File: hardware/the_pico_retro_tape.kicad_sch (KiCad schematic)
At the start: 6 parts, among them U1 Pico

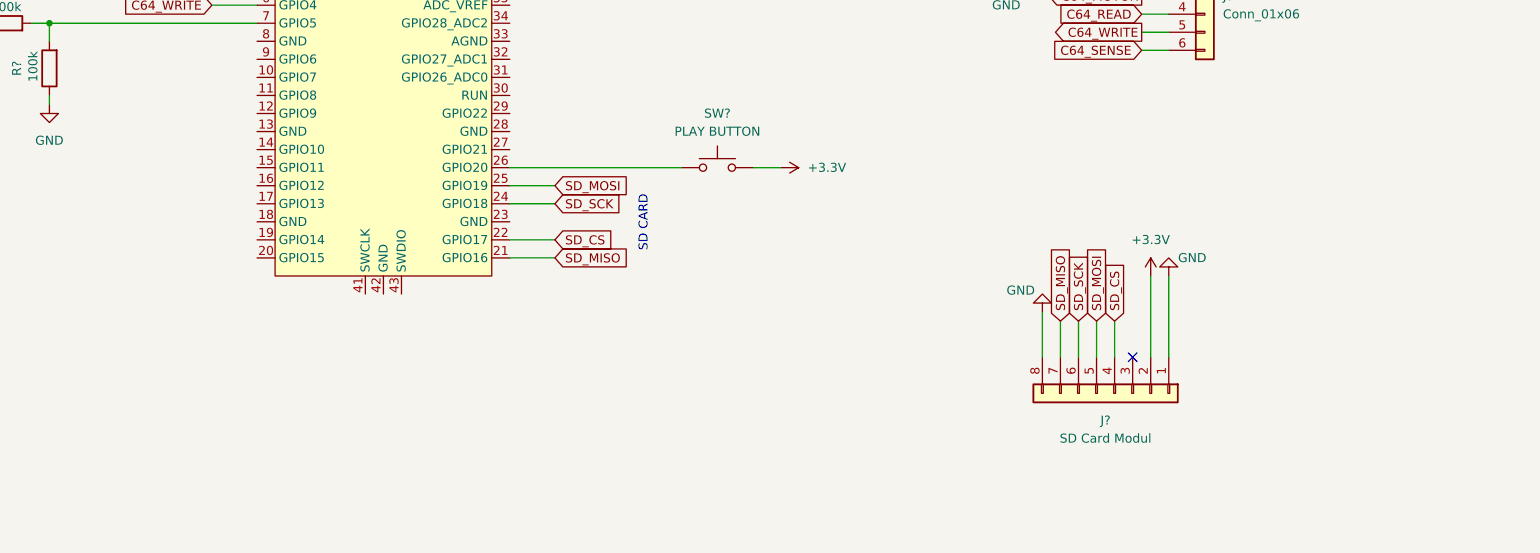
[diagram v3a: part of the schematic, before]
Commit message: hardware: added the tft display st7735 on spi1
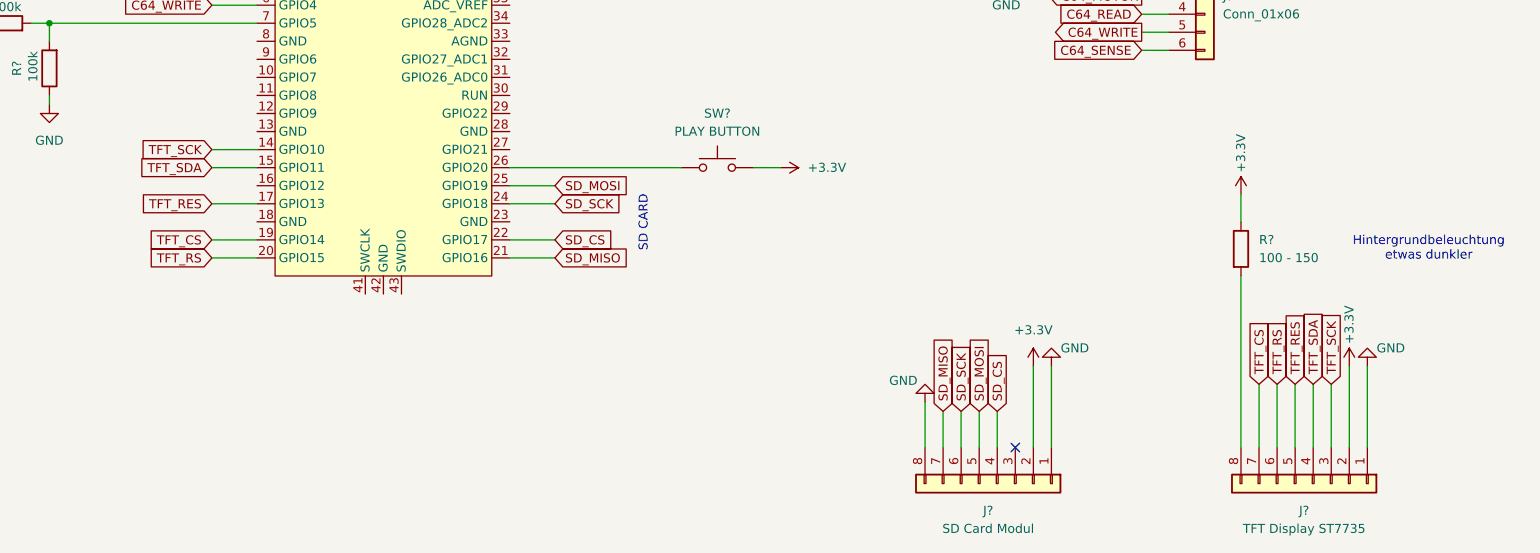
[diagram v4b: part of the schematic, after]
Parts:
- added J?: TFT Display ST7735, symbol Connector_Generic:Conn_01x08
- added R?: 100 - 150, symbol Device:R
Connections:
- net +3.3V: now also J?.2 (Pin_2), R?.1
- net GND: now also J?.1 (Pin_1)
- net TFT_SCK: now reaches U1.14 (GPIO10)
- net TFT_SCK: now also J?.3 (Pin_3)
- net TFT_SDA: now reaches U1.15 (GPIO11)
- net TFT_SDA: now also J?.4 (Pin_4)
- net TFT_RES: now reaches U1.17 (GPIO13)
- net TFT_RES: now also J?.5 (Pin_5)
- net TFT_CS: now reaches U1.19 (GPIO14)
- net TFT_CS: now also J?.7 (Pin_7)
- net TFT_RS: now reaches U1.20 (GPIO15)
- net TFT_RS: now also J?.6 (Pin_6)
- new net: J?.8 (Pin_8), R?.2
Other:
- note added: "Hintergrundbeleuchtung etwas dunkler"
- moved on the sheet: J?

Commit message: hardware: change tft vcc and led from 3.3v to 5v
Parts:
- R?: value 100 - 150 -> 150
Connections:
- net +3.3V: no longer J?.2 (Pin_2), R?.1
- net +5V: now also J?.2 (Pin_2), J?.2 (Pin_2), R?.1
- no-connect marks 2 -> 1
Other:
- note removed: "Hintergrundbeleuchtung etwas dunkler"
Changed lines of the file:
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@@
 		(at 195.58 123.19)
 	)
-	(no_connect
-		(at 217.17 57.15)
-	)
 	(wire
 		(pts
@@
 		(pts
 			(xy 245.11 111.76) (xy 245.11 123.19)
+		)
+		(stroke
+			(width 0)
+			(type default)
+		)
+	)
+	(wire
+		(pts
+			(xy 213.36 57.15) (xy 217.17 57.15)
 		)
 		(stroke
@@
 		(exclude_from_sim no)
 		(at 143.256 91.694 90)
-		(effects
-			(font
-				(size 1.27 1.27)
-			)
-		)
-	)
-	(text "Hintergrundbeleuchtung\netwas dunkler"
-		(exclude_from_sim no)
-		(at 253.746 95.25 0)
 		(effects
 			(font
@@
 	)
 	(symbol
+		(lib_id "power:+5V")
+		(at 213.36 57.15 90)
+		(unit 1)
+		(exclude_from_sim no)
+		(in_bom yes)
+		(on_board yes)
+		(dnp no)
+		(fields_autoplaced yes)
+		(property "Reference" "#PWR013"
+			(at 217.17 57.15 0)
+			(effects
+				(font
+					(size 1.27 1.27)
+				)
+				(hide yes)
+			)
+		)
+		(property "Value" "+5V"
+			(at 209.55 57.1499 90)
+			(effects
+				(font
+					(size 1.27 1.27)
+				)
+				(justify left)
+			)
+		)
+		(property "Footprint" ""
+			(at 213.36 57.15 0)
+			(effects
+				(font
+					(size 1.27 1.27)
+				)
+				(hide yes)
+			)
+		)
+		(property "Datasheet" ""
+			(at 213.36 57.15 0)
+			(effects
+				(font
+					(size 1.27 1.27)
+				)
+				(hide yes)
+			)
+		)
+		(property "Description" "Power symbol creates a global label with name \"+5V\""
+			(at 213.36 57.15 0)
+			(effects
+				(font
+					(size 1.27 1.27)
+				)
+				(hide yes)
+			)
+		)
+		(pin "1"
+		)
+		(instances
+			(project "the_pico_retro_tape"
+				(path "/58eb91ea-7f3f-48ec-bf75-2e4d8bc1bbc2"
+					(reference "#PWR013")
+					(unit 1)
+				)
+			)
+		)
+	)
+	(symbol
 		(lib_id "power:+3.3V")
 		(at 133.35 58.42 270)
@@
 	)
 	(symbol
-		(lib_id "power:+3.3V")
-		(at 227.33 87.63 0)
-		(unit 1)
-		(exclude_from_sim no)
-		(in_bom yes)
-		(on_board yes)
-		(dnp no)
-		(property "Reference" "#PWR012"
-			(at 227.33 91.44 0)
-			(effects
-				(font
-					(size 1.27 1.27)
-				)
-				(hide yes)
-			)
-		)
-		(property "Value" "+3.3V"
-			(at 227.33 81.788 90)
-			(effects
-				(font
-					(size 1.27 1.27)
-				)
-			)
-		)
-		(property "Footprint" ""
-			(at 227.33 87.63 0)
-			(effects
-				(font
-					(size 1.27 1.27)
-				)
-				(hide yes)
-			)
-		)
-		(property "Datasheet" ""
-			(at 227.33 87.63 0)
-			(effects
-				(font
-					(size 1.27 1.27)
-				)
-				(hide yes)
-			)
-		)
-		(property "Description" "Power symbol creates a global label with name \"+3.3V\""
-			(at 227.33 87.63 0)
-			(effects
-				(font
-					(size 1.27 1.27)
-				)
-				(hide yes)
-			)
-		)
-		(pin "1"
-		)
-		(instances
-			(project "the_pico_retro_tape"
-				(path "/58eb91ea-7f3f-48ec-bf75-2e4d8bc1bbc2"
-					(reference "#PWR012")
-					(unit 1)
-				)
-			)
-		)
-	)
-	(symbol
 		(lib_id "Switch:SW_Push")
 		(at 153.67 83.82 0)
@@
 				(path "/58eb91ea-7f3f-48ec-bf75-2e4d8bc1bbc2"
 					(reference "SW?")
+					(unit 1)
+				)
+			)
+		)
+	)
+	(symbol
+		(lib_id "power:+5V")
+		(at 242.57 111.76 0)
+		(unit 1)
+		(exclude_from_sim no)
+		(in_bom yes)
+		(on_board yes)
+		(dnp no)
+		(property "Reference" "#PWR012"
+			(at 242.57 115.57 0)
+			(effects
+				(font
+					(size 1.27 1.27)
+				)
+				(hide yes)
+			)
+		)
+		(property "Value" "+5V"
+			(at 242.57 106.68 90)
+			(effects
+				(font
+					(size 1.27 1.27)
+				)
+			)
+		)
+		(property "Footprint" ""
+			(at 242.57 111.76 0)
+			(effects
+				(font
+					(size 1.27 1.27)
+				)
+				(hide yes)
+			)
+		)
+		(property "Datasheet" ""
+			(at 242.57 111.76 0)
+			(effects
+				(font
+					(size 1.27 1.27)
+				)
+				(hide yes)
+			)
+		)
+		(property "Description" "Power symbol creates a global label with name \"+5V\""
+			(at 242.57 111.76 0)
+			(effects
+				(font
+					(size 1.27 1.27)
+				)
+				(hide yes)
+			)
+		)
+		(pin "1"
+		)
+		(instances
+			(project "the_pico_retro_tape"
+				(path "/58eb91ea-7f3f-48ec-bf75-2e4d8bc1bbc2"
+					(reference "#PWR012")
 					(unit 1)
 				)
@@
 	)
 	(symbol
-		(lib_id "power:+3.3V")
-		(at 242.57 111.76 0)
-		(unit 1)
-		(exclude_from_sim no)
-		(in_bom yes)
-		(on_board yes)
-		(dnp no)
-		(property "Reference" "#PWR011"
-			(at 242.57 115.57 0)
-			(effects
-				(font
-					(size 1.27 1.27)
-				)
-				(hide yes)
-			)
-		)
-		(property "Value" "+3.3V"
-			(at 242.57 105.918 90)
-			(effects
-				(font
-					(size 1.27 1.27)
-				)
-			)
-		)
-		(property "Footprint" ""
-			(at 242.57 111.76 0)
-			(effects
-				(font
-					(size 1.27 1.27)
-				)
-				(hide yes)
-			)
-		)
-		(property "Datasheet" ""
-			(at 242.57 111.76 0)
-			(effects
-				(font
-					(size 1.27 1.27)
-				)
-				(hide yes)
-			)
-		)
-		(property "Description" "Power symbol creates a global label with name \"+3.3V\""
-			(at 242.57 111.76 0)
-			(effects
-				(font
-					(size 1.27 1.27)
-				)
-				(hide yes)
-			)
-		)
-		(pin "1"
-		)
-		(instances
-			(project "the_pico_retro_tape"
-				(path "/58eb91ea-7f3f-48ec-bf75-2e4d8bc1bbc2"
-					(reference "#PWR011")
-					(unit 1)
-				)
-			)
-		)
-	)
-	(symbol
 		(lib_id "Device:R")
 		(at 227.33 95.25 0)
@@
 			)
 		)
-		(property "Value" "100 - 150"
+		(property "Value" "150"
 			(at 229.87 96.5199 0)
 			(effects
@@
 					(unit 1)
 				)
+			)
+		)
+	)
+	(symbol
+		(lib_id "power:+5V")
+		(at 227.33 87.63 0)
+		(unit 1)
+		(exclude_from_sim no)
+		(in_bom yes)
+		(on_board yes)
+		(dnp no)
+		(fields_autoplaced yes)
+		(property "Reference" "#PWR011"
+			(at 227.33 91.44 0)
+			(effects
+				(font
+					(size 1.27 1.27)
+				)
+				(hide yes)
+			)
+		)
+		(property "Value" "+5V"
+			(at 227.33 82.55 0)
+			(effects
+				(font
+					(size 1.27 1.27)
+				)
+			)
+		)
+		(property "Footprint" ""
+			(at 227.33 87.63 0)
+			(effects
+				(font
+					(size 1.27 1.27)
+				)
+				(hide yes)
+			)
+		)
+		(property "Datasheet" ""
+			(at 227.33 87.63 0)
+			(effects
+				(font
+					(size 1.27 1.27)
+				)
+				(hide yes)
+			)
+		)
+		(property "Description" "Power symbol creates a global label with name \"+5V\""
+			(at 227.33 87.63 0)
+			(effects
+				(font
+					(size 1.27 1.27)
+				)
+				(hide yes)
+			)
+		)
+		(pin "1"
+		)
+		(instances
+			(project "the_pico_retro_tape"
+				(path "/58eb91ea-7f3f-48ec-bf75-2e4d8bc1bbc2"
+					(reference "#PWR011")
+					(unit 1)
+				)

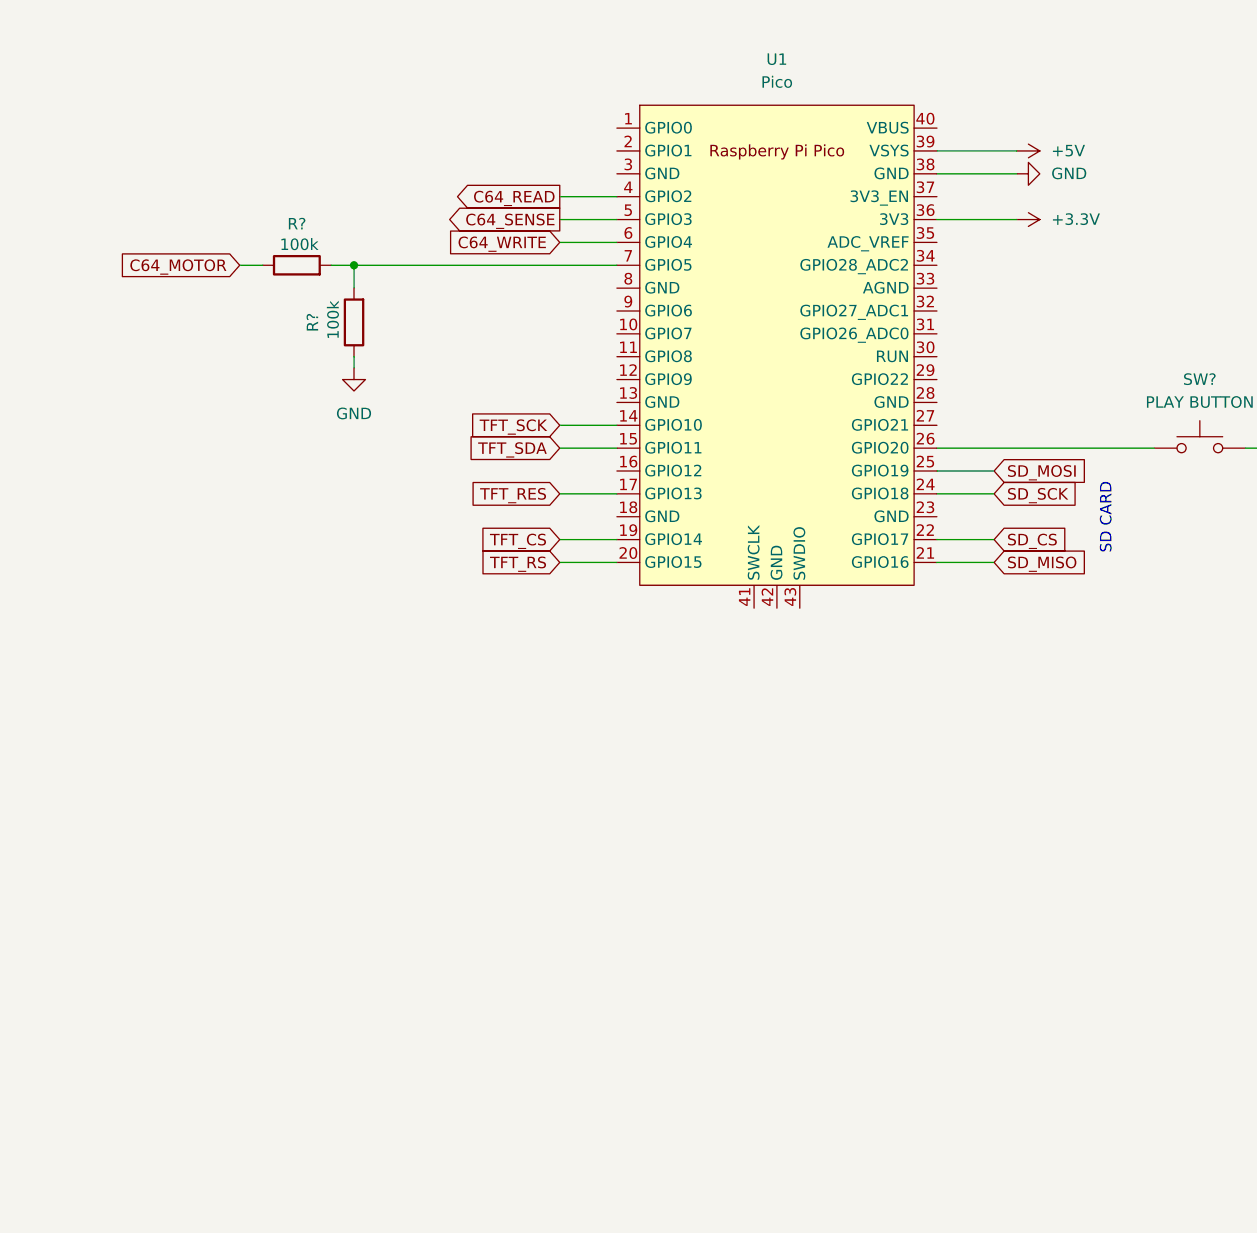
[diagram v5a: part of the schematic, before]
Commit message: hardware: added 3 buttons for gui
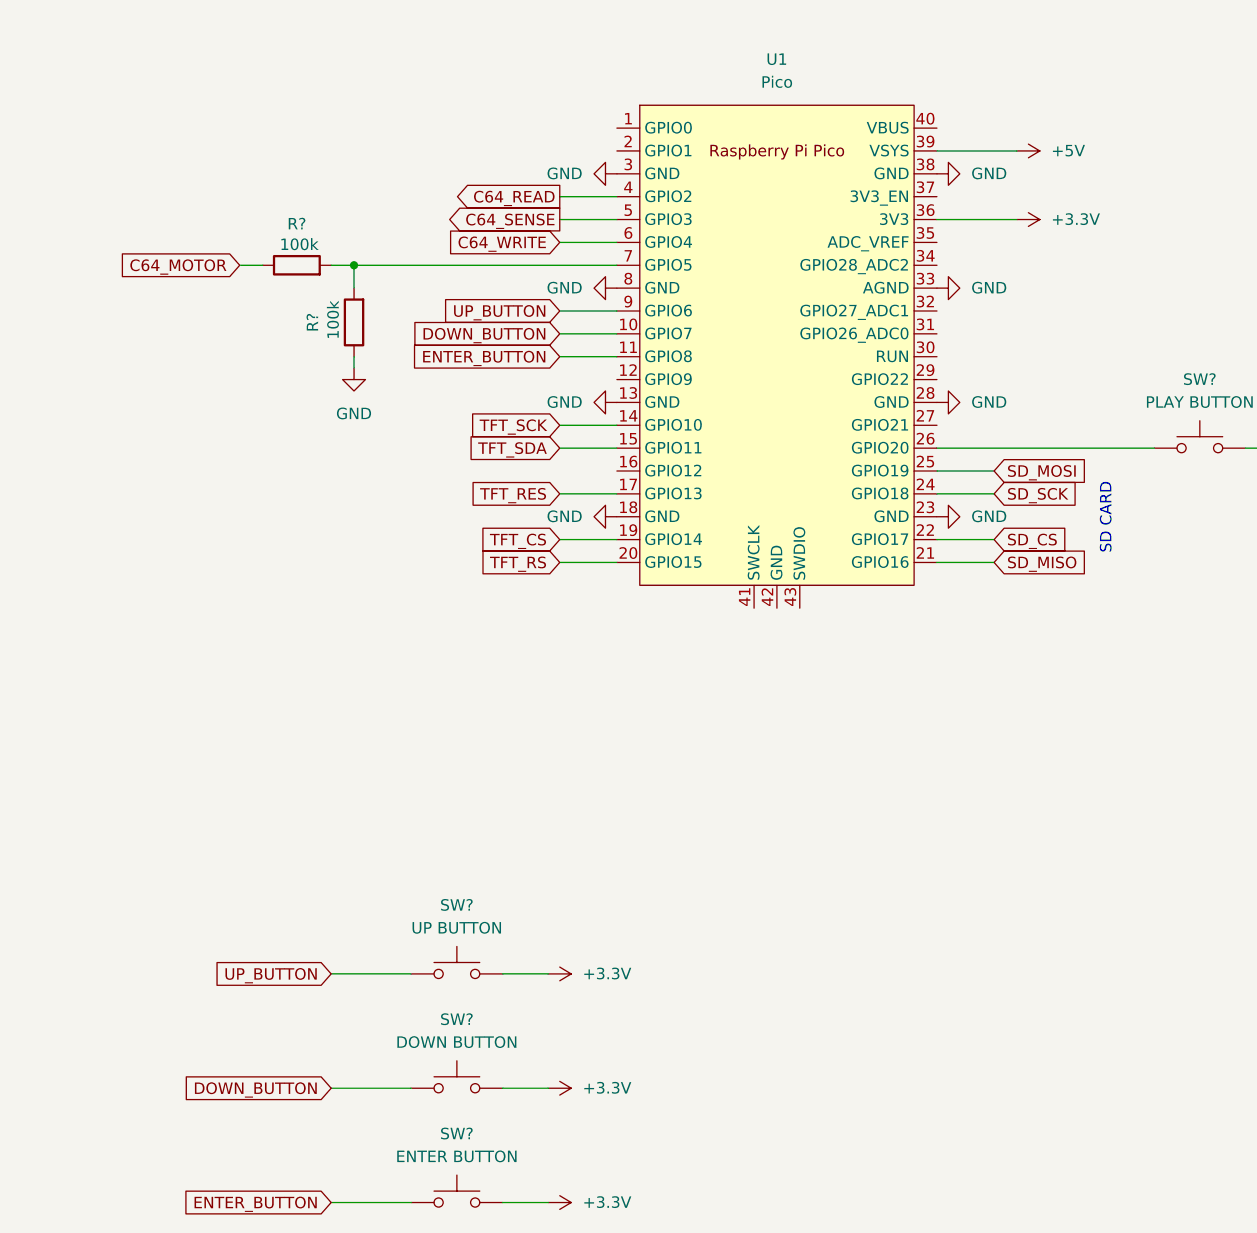
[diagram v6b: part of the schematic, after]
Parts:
- added SW?: UP BUTTON, symbol Switch:SW_Push
- added SW?: DOWN BUTTON, symbol Switch:SW_Push
- added SW?: ENTER BUTTON, symbol Switch:SW_Push
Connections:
- net +3.3V: now also SW?.2, SW?.2, SW?.2
- net GND: now also U1.13 (GND), U1.18 (GND), U1.23 (GND), U1.28 (GND), U1.3 (GND), U1.33 (AGND), U1.8 (GND)
- net DOWN_BUTTON: now reaches U1.10 (GPIO7)
- net DOWN_BUTTON: now also SW?.1
- net ENTER_BUTTON: now reaches U1.11 (GPIO8)
- net ENTER_BUTTON: now also SW?.1
- net UP_BUTTON: now reaches U1.9 (GPIO6)
- net UP_BUTTON: now also SW?.1
